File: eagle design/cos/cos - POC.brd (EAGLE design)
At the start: 35 x 63 mm, 103 parts, among them IC1 SQJ952EP-T1_GE3, IC10 PBRC8.00GR50X000, IC11 LM74670QDGKRQ1, IC12 LM74670QDGKRQ1, IC13 SQJ886EP-T1_GE3, IC15 MCP23S08-E/ML, IC16 LDK320M50R, IC17 MCP2515, IC18 LM74670QDGKRQ1, IC19 MCP2561-2, IC2 SQJ952EP-T1_GE3, IC20 AD5160BRJZ5-R2, IC21 MP3221GJ-P, IC3 SQJ952EP-T1_GE3, IC4 TPS630702RNMT, IC5 LM74670QDGKRQ1, IC6 FDMQ8403, IC7 LMP92064SD/NOPB, IC8 ATTINY4313-MMH, IC9 LM74670QDGKRQ1

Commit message: - further layout work
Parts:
- removed TP9: Li-Ion Cell +, testpad:P1-13
- C1, C2: value 10μF -> 3300μF / 35V / ultralow ESR; device rcl:C0805 -> rcl:E1,8-4
- C3: device rcl:C0603 -> rcl:C0805
- C4: value 3300μF / 35V / ultralow ESR -> 10μF; device rcl:E1,8-4 -> rcl:C0805
- C5: value 3300μF / 35V / ultralow ESR -> 10μF; device rcl:E1,8-4 -> rcl:C0603
- IC3: value SQJ952EP-T1_GE3 -> TPS630702RNMT; device SQJ952EP-T1_GE3 - Dual N-Fet:SO-8L -> TPS630701 - Buck Boost 5V regulator:VQFN
- IC4: value TPS630702RNMT -> LM74670QDGKRQ1; device TPS630701 - Buck Boost 5V regulator:VQFN -> LM74670 - Smart Diode Rectifier Controller:VSSOP-8
- IC5: value LM74670QDGKRQ1 -> SQJ952EP-T1_GE3; device LM74670 - Smart Diode Rectifier Controller:VSSOP-8 -> SQJ952EP-T1_GE3 - Dual N-Fet:SO-8L
- R2: value 10k -> 47k
- R4: value 47k -> 100k
- R7: value 100k -> 10k
- moved R4 84.8 mm to (49.5, -20.0), flipped to the top
- moved C3 79.6 mm to (95.2, 33.0), turned to 0 degrees
- moved TP5 78.3 mm to (107.2, 30.8), turned to 270 degrees
- moved C7 77.4 mm to (101.8, 27.2)
- moved L1 77.4 mm to (101.2, 33.0)
- moved R13 77.4 mm to (101.8, 28.5)
- moved TP6 77.0 mm to (107.2, 32.2), turned to 270 degrees
- moved C10 76.6 mm to (104.2, 33.5)
- moved C11 76.6 mm to (106.2, 33.5)
- moved C13 76.6 mm to (108.2, 33.5)
- moved C18 75.7 mm to (107.2, 29.5)
- moved R7 70.3 mm to (96.5, 37.2), flipped to the bottom
- moved IC4 67.2 mm to (105.0, 49.0)
- moved C2 66.1 mm to (103.0, 45.0), turned to 0 degrees
- moved C1 60.9 mm to (107.2, 45.0), turned to 180 degrees
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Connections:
- net 5V0_LDO: now also R3.2; no longer R2.2
- net 5V0_TP-IN: now also IC3.5-FB, IC3.7-VOUT, IC3.8-VOUT, IC3.VOUT; no longer IC4.5-FB, IC4.7-VOUT, IC4.8-VOUT, IC4.VOUT
- net D1_VCAPH: now also IC4.VCAPH; no longer IC5.VCAPH
- net D1_VCAPL: now also IC4.VCAPL; no longer IC5.VCAPL
- net DELON_1: now also IC5.D1_1, IC5.D1_2, IC5.D1_3; no longer IC3.D1_1, IC3.D1_2, IC3.D1_3
- net DYNAMO_2: now also IC5.D2_1, IC5.D2_2, IC5.D2_3; no longer IC3.D2_1, IC3.D2_2, IC3.D2_3
- net DYNAMO_2_C: now also C1.-, IC4.ANODE; no longer C4.-, IC5.ANODE
- net EN: now also IC3.14-EN; no longer IC4.14-EN
- net GATE_D1: now also IC4.GATE_DRIVE, IC4.GATE_PULLD; no longer IC5.GATE_DRIVE, IC5.GATE_PULLD
- net GATE_DELON: now also IC5.G1, IC5.G2, R7.2; no longer IC3.G1, IC3.G2, R3.2
- net GATE_GRAETZ: now also R3.1; no longer R2.1
- net GND: now also C4.2, C5.2, IC3.10-PGND, IC3.15-VSEL, IC3.4-GND, IC3.6-FB2, R7.1; no longer C1.2, C2.2, IC4.10-PGND, IC4.15-VSEL, IC4.4-GND, IC4.6-FB2, R3.1, TP9.TP
- net N$1: now also IC3.11-L1; no longer IC4.11-L1
- net N$14: now also R4.1, R5.2; no longer R5.1, R6.2
- net N$20: now also IC5.S1, IC5.S2; no longer IC3.S1, IC3.S2
- net N$5: now also IC3.9-L2; no longer IC4.9-L2
- net PG: now also IC3.2-PG; no longer IC4.2-PG
- net PS/SYNC: now also IC3.1-PS/S; no longer IC4.1-PS/S
- net TUNING_CAP_DRAIN: now also C2.-; no longer C5.-
- net TUNIN_CAP2_BIAS: now also C1.+, C2.+, R2.1; no longer C4.+, C5.+, R4.1
- net VAUX: now also IC3.3-VAUX; no longer IC4.3-VAUX
- net V_DC_TP-IN: now also IC4.CATHODE, R2.2; no longer IC5.CATHODE, R4.2
- net V_REGULATED_TP-OUT: now also C4.1, C5.1, IC3.12-VIN, IC3.13-VIN, IC3.VIN; no longer C1.1, C2.1, IC4.12-VIN, IC4.13-VIN, IC4.VIN
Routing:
- net DYNAMO_2: track 19.0 -> 42.5 mm, vias 9 -> 10
- net V_REGULATED_TP-IN: track 15.3 -> 38.7 mm, vias 7 -> 6
- net DYNAMO_2_C: track 40.9 -> 63.3 mm
- net V_DC_TP-OUT: track 9.54 -> 20.7 mm, vias 0 -> 2
- net GATE_TUNING-CAP: track 4.27 -> 12.3 mm
- net GATE_GRAETZ: track 4.27 -> 11.7 mm
- net V_LI-ION_BATTERY: track 7.71 -> 15.1 mm
- net GATE_DELON: track 4.27 -> 11.4 mm
- net V_REGULATED_TP-OUT: track 5.35 -> 11.6 mm
- net TUNING_CAP_DRAIN: track 8.30 -> 12.8 mm
- net DELON_1: track 9.80 -> 14.0 mm
- net V_DC_TP-IN: track 31.1 -> 34.4 mm
- net 5V0_TP-IN: track 14.5 -> 17.8 mm, vias 3 -> 4
- net DYNAMO_1: track 23.4 -> 26.4 mm
- net IDEAL_DIODE_GATE: track 6.52 -> 9.50 mm
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
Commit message: - further work on schematic
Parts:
- removed C22: 0.1μF, rcl:C0402
- removed IC11: LM74670QDGKRQ1, LM74670 - Smart Diode Rectifier Controller:VSSOP-8
- removed IC13: SQJ886EP-T1_GE3, SQJ886EP - N-FET:SO-8L
- added C36, C37: 0.1μF, rcl:C0402
- added IC22: SQJ952EP-T1_GE3, SQJ952EP-T1_GE3 - Dual N-Fet:SO-8L
- added IC23, IC24: LM74670QDGKRQ1, LM74670 - Smart Diode Rectifier Controller:VSSOP-8
- IC14: value (none) -> MCP73871-2CCI/ML
- moved TP11 16.0 mm to (86.2, 45.2)
- moved TP12 16.0 mm to (86.2, 43.8)
- moved D5 0.75 mm to (111.2, 31.5)
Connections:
- removed net D5_VCAPH: C22.2, IC11.VCAPH
- removed net D5_VCAPL: C22.1, IC11.VCAPL
- removed net DYNAMO_2: D3.A, IC1.D2_1, IC1.D2_2, IC1.D2_3, IC2.D1_1, IC2.D1_2, IC2.D1_3, IC5.D2_1, IC5.D2_2, IC5.D2_3
- removed net DYNAMO_2_C: C1.-, D1.A, IC2.D2_1, IC2.D2_2, IC2.D2_3, IC4.ANODE, IC6.3_S1/D2, IC6.S1/D2, IC9.CATHODE, TP1.TP
- removed net IDEAL_DIODE_GATE: IC11.GATE_DRIVE, IC11.GATE_PULLD, IC13.G
- removed net TUNING_CAP_DRAIN: C2.-, IC1.D1_1, IC1.D1_2, IC1.D1_3
- new net AFTER_SW_BEFORE_TUNING_CAP: C1.-, IC1.D2_1, IC1.D2_2, IC1.D2_3
- new net DYNAMO_2_AFTER_SW: C2.-, D3.A, IC2.D1_1, IC2.D1_2, IC2.D1_3, IC5.D2_1, IC5.D2_2, IC5.D2_3
- new net DYNAMO_2_BEFORE_SW: D1.A, IC1.D1_1, IC1.D1_2, IC1.D1_3, IC2.D2_1, IC2.D2_2, IC2.D2_3, IC4.ANODE, IC6.3_S1/D2, IC6.S1/D2, IC9.CATHODE, TP1.TP
- new net D_SMOOTH_VCAP: C36.1, IC23.VCAPL
- new net D_SMOOTH_VCAPH: C36.2, IC23.VCAPH
- new net D_VLIION_VCAPH: C37.2, IC24.VCAPH
- new net D_VLIION_VCAPL: C37.1, IC24.VCAPL
- new net GATE_DIODE_SMOOTH: IC22.G1, IC23.GATE_DRIVE, IC23.GATE_PULLD
- new net GATE_DIODE_V_LIION: IC22.G2, IC24.GATE_DRIVE, IC24.GATE_PULLD
- net V_DC_TP-OUT: now also IC22.S1, IC23.ANODE; no longer IC11.ANODE, IC13.S1, IC13.S2, IC13.S3
- net V_LI-ION_BATTERY: now also IC22.S2, IC24.ANODE
- net V_REGULATED_TP-IN: now also IC23.CATHODE; no longer IC11.CATHODE, IC13.D1, IC13.D2
- net V_REGULATED_TP-OUT: now also IC22.D1_1, IC22.D1_2, IC22.D1_3, IC22.D2_1, IC22.D2_2, IC22.D2_3, IC24.CATHODE
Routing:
- net DYNAMO_2_C: track 63.3 -> 0.00 mm, vias 8 -> 0
- net DYNAMO_2_BEFORE_SW: track 0.00 -> 50.9 mm, vias 0 -> 5
- net DYNAMO_2: track 42.5 -> 0.00 mm, vias 10 -> 0
- net DYNAMO_2_AFTER_SW: track 0.00 -> 39.2 mm, vias 0 -> 10
- net V_REGULATED_TP-IN: track 38.7 -> 0.11 mm, vias 6 -> 0
- net V_DC_TP-OUT: track 20.7 -> 0.00 mm, vias 2 -> 0
- net V_REGULATED_TP-OUT: track 11.6 -> 26.5 mm
- net TUNING_CAP_DRAIN: track 12.8 -> 0.00 mm, vias 3 -> 0
- net IDEAL_DIODE_GATE: track 9.50 -> 0.00 mm, vias 2 -> 0
- net GATE_DIODE_SMOOTH: track 0.00 -> 7.38 mm
- net GATE_DIODE_V_LIION: track 0.00 -> 7.03 mm
- net V_LI-ION_BATTERY: track 15.1 -> 17.5 mm
- net D5_VCAPL: track 2.27 -> 0.00 mm, vias 1 -> 0
- net D5_VCAPH: track 1.65 -> 0.00 mm, vias 1 -> 0
- net COMP_IN: track 3.24 -> 2.49 mm

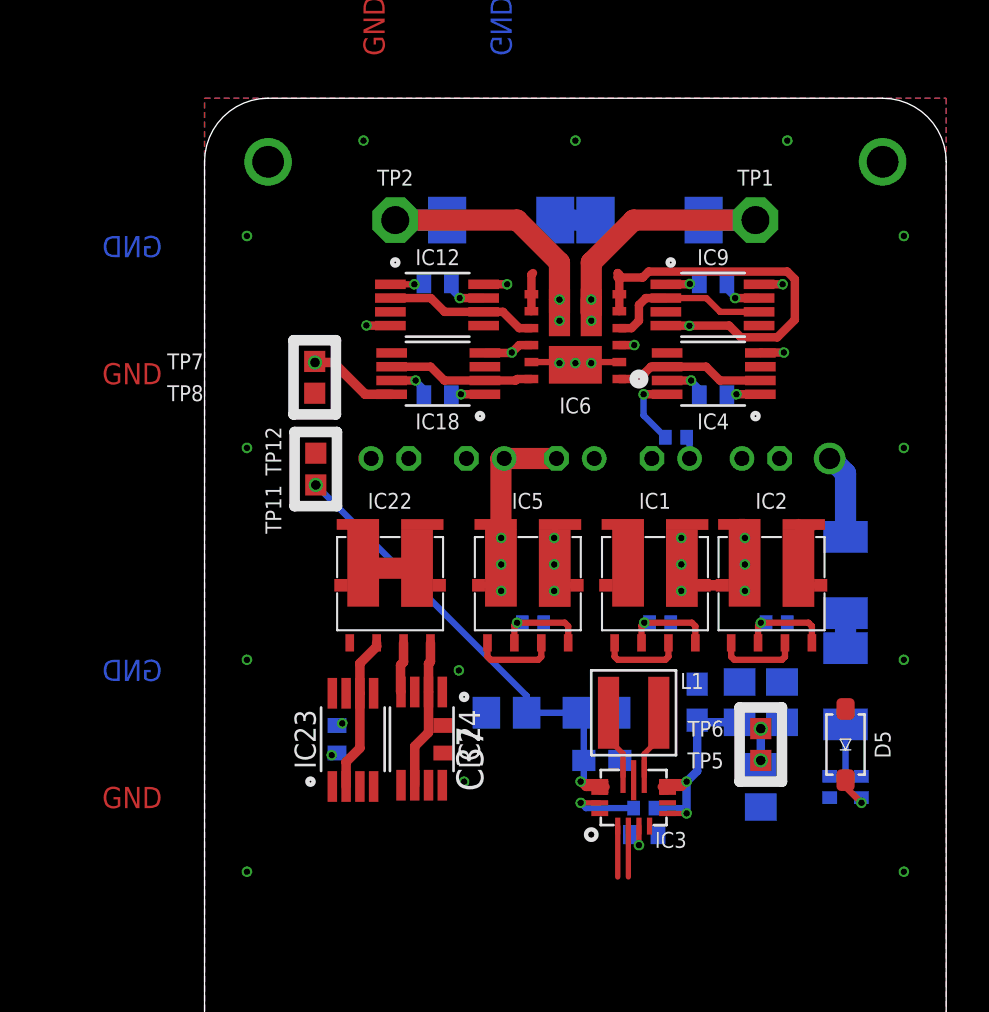
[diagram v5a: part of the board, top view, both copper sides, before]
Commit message: - further work on schematic:routed bridge rectifier segment - added TPS630701 - Buck-Boost Converter 5V out fixed datasheet
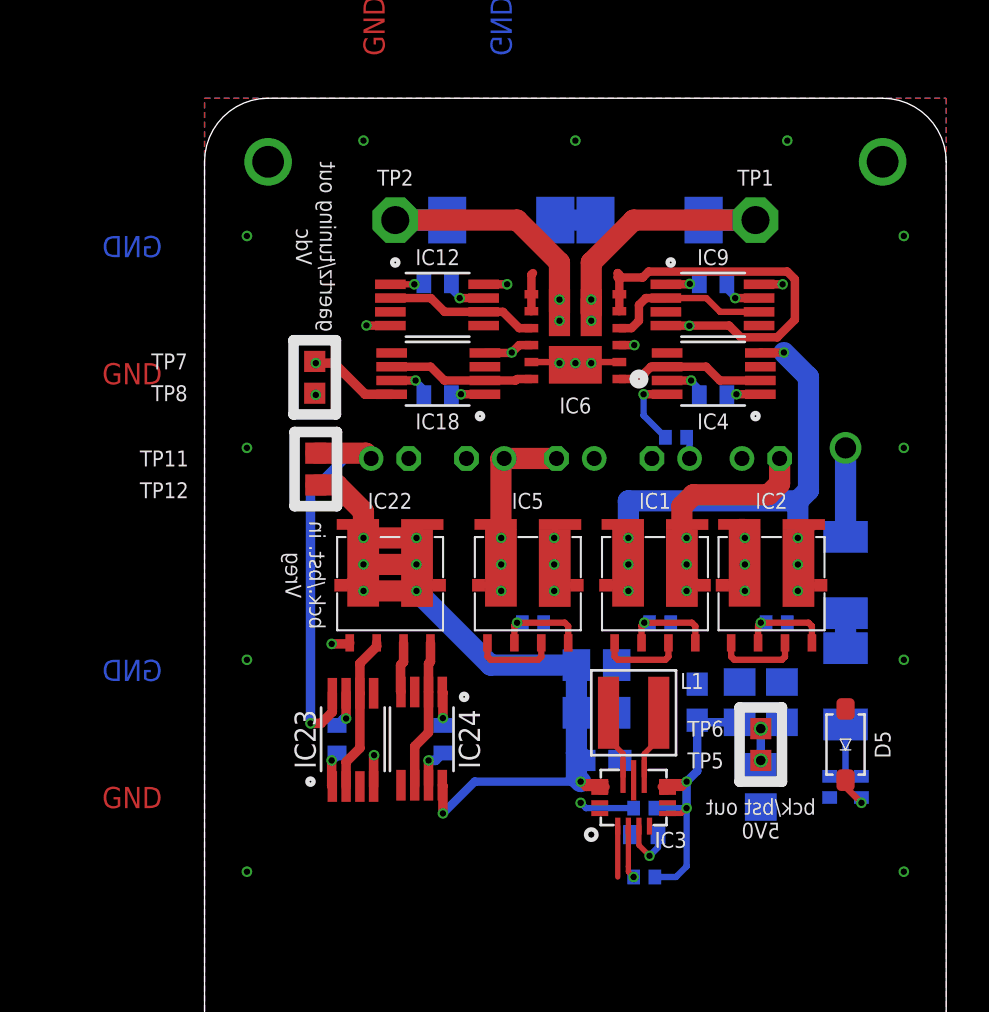
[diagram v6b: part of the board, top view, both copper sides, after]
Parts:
- added R27: 100k, rcl:R0402
- moved C3 4.81 mm to (99.5, 35.2), turned to 180 degrees
- flipped C37 to the bottom
- turned C7 to 0 degrees
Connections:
- new net EN2: IC21.4_EN, R23.1
- net 5V0_TP-IN: now also R27.2
- net EN: no longer IC21.4_EN, IC3.14-EN, R23.1
- net PG: now also R27.1
- net V_REGULATED_TP-OUT: now also IC3.14-EN
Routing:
- net V_REGULATED_TP-OUT: track 26.5 -> 52.4 mm, vias 2 -> 8
- net V_DC_TP-OUT: track 0.00 -> 20.5 mm, vias 0 -> 3
- net V_REGULATED_TP-IN: track 0.11 -> 19.3 mm, vias 0 -> 1
- net AFTER_SW_BEFORE_TUNING_CAP: track 0.00 -> 15.5 mm, vias 0 -> 3
- net DYNAMO_2_BEFORE_SW: track 50.9 -> 59.8 mm, vias 5 -> 11
- net 5V0_TP-IN: track 18.0 -> 22.2 mm
- net D_VLIION_VCAPH: track 0.00 -> 1.99 mm, vias 0 -> 1
- net EN: track 4.47 -> 2.60 mm, vias 2 -> 1
- net D_SMOOTH_VCAPH: track 0.00 -> 1.76 mm, vias 0 -> 1
- net D_SMOOTH_VCAP: track 0.00 -> 1.70 mm, vias 0 -> 1
- net D_VLIION_VCAPL: track 0.00 -> 1.59 mm, vias 0 -> 1
- net VAUX: track 1.57 -> 2.77 mm
- net EN2: track 0.00 -> 0.97 mm, vias 0 -> 1
- net DYNAMO_2_AFTER_SW: track 39.2 -> 39.8 mm, vias 10 -> 7
- net V_DC_TP-IN: track 34.4 -> 34.9 mm
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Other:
- board text added: "bck./bst. in Vreg"
- board text added: "bck/bst out 5V0"
- board text added: "gaertz/tuning out Vdc"

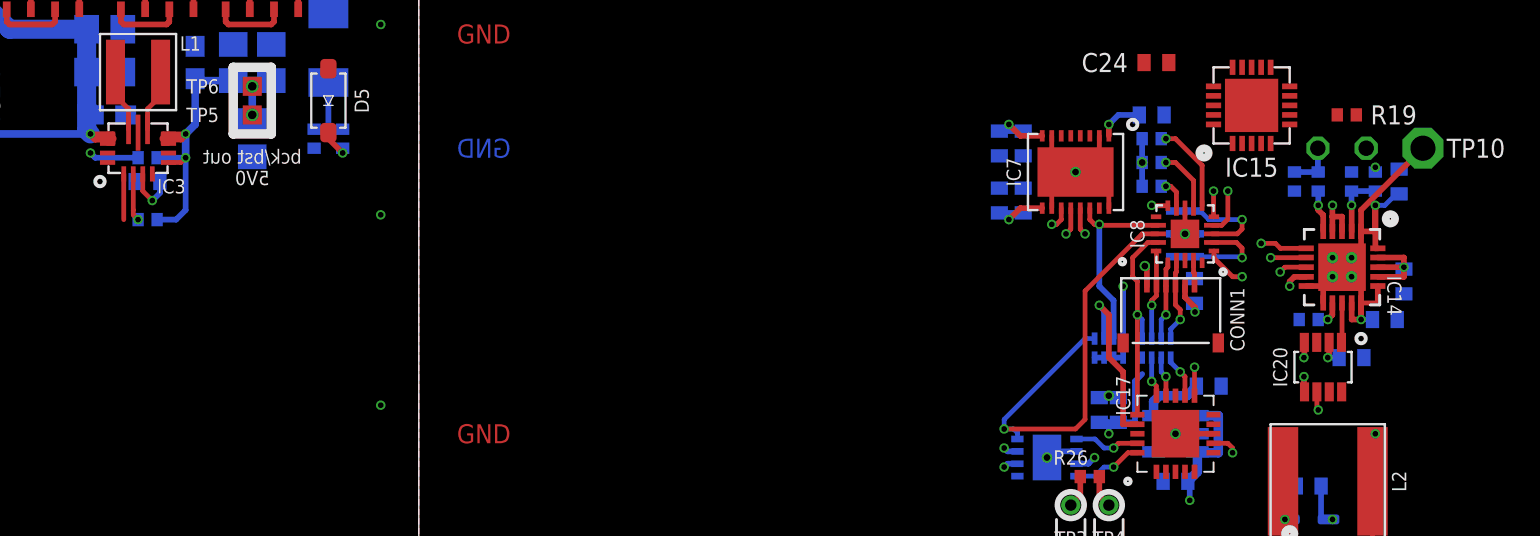
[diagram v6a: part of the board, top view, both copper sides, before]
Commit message: - further work on schematic: reassigned ps/sync to a 16bit timer capable GPIO
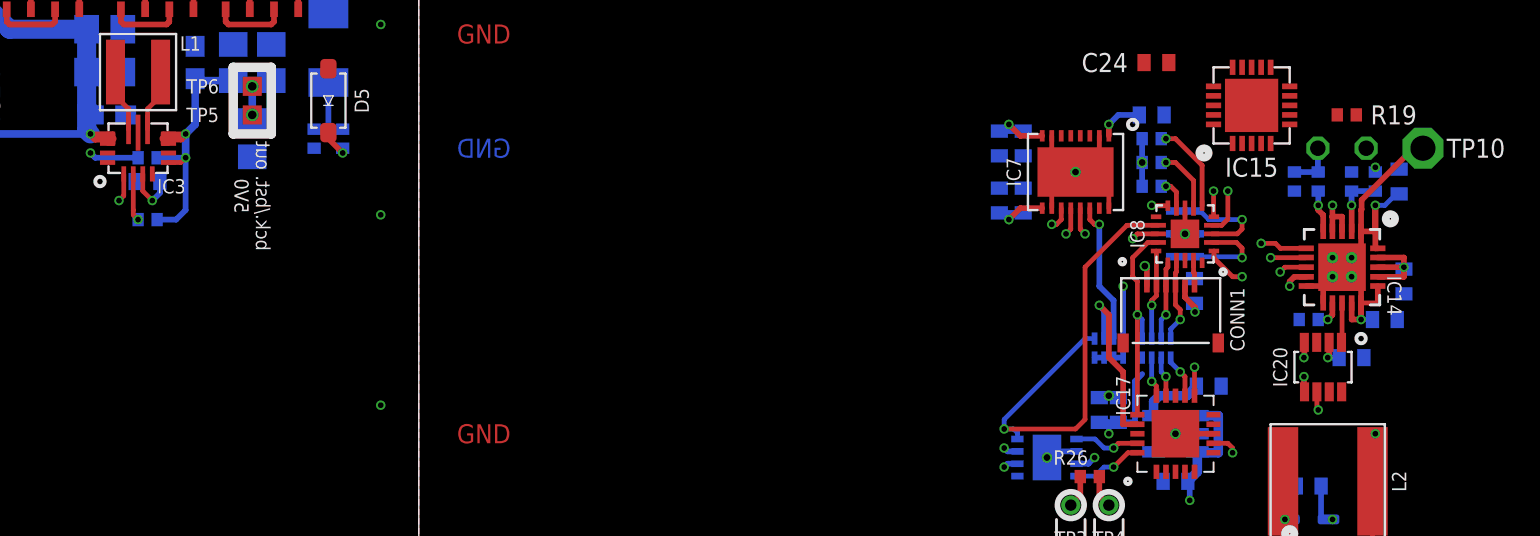
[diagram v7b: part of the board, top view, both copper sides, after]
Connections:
- removed net MCP23S08_GP7: IC15.16_GP7
- net LMP92064SD_CS: now also IC15.16_GP7; no longer IC8.12
- net PS/SYNC: now also IC8.13
- net STBY: now also IC8.12; no longer IC8.13
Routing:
- net PS/SYNC: track 2.40 -> 12.9 mm, vias 0 -> 2
- net LMP92064SD_CS: track 10.6 -> 7.58 mm
- net STBY: track 24.4 -> 25.3 mm
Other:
- board text added: "bck./bst. out 5V0"
- board text removed: "bck/bst out 5V0"
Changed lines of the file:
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@@
 <text x="102" y="-3" size="1" layer="16" font="vector" rot="MR90" align="center-right">GND</text>
 <text x="106" y="-3" size="1" layer="2" font="vector" rot="R90" align="center-right">GND</text>
-<text x="107.25" y="28" size="0.75" layer="21" rot="MR0" align="center">bck/bst out
+<text x="107.25" y="26.5" size="0.75" layer="21" rot="MR270" align="center">bck./bst. out
 5V0</text>
 <text x="85.75" y="39.5" size="0.75" layer="21" rot="MR270" align="center">bck./bst. in
@@
 <wire x1="151" y1="19" x2="146.75" y2="14.75" width="0.25" layer="16"/>
 <wire x1="146.75" y1="14.75" x2="146.75" y2="14.25" width="0.25" layer="16"/>
-<contactref element="IC8" pad="13"/>
-<wire x1="154.85" y1="24.5" x2="154" y2="24.5" width="0.25" layer="1"/>
-<wire x1="151" y1="21.5" x2="154" y2="24.5" width="0.25" layer="1"/>
 <wire x1="146.75" y1="14.25" x2="150.5" y2="14.25" width="0.25" layer="1"/>
 <wire x1="150.5" y1="14.25" x2="151" y2="14.75" width="0.25" layer="1"/>
-<wire x1="151" y1="14.75" x2="151" y2="21.5" width="0.25" layer="1"/>
+<wire x1="151" y1="22.75" x2="151" y2="14.75" width="0.25" layer="1"/>
+<contactref element="IC8" pad="12"/>
+<wire x1="154.85" y1="24.95" x2="153.2" y2="24.95" width="0.25" layer="1"/>
+<wire x1="153.2" y1="24.95" x2="151" y2="22.75" width="0.25" layer="1"/>
 </signal>
 <signal name="5V0_TP-OUT" class="2">
@@
 <wire x1="166.1" y1="20" x2="165.5" y2="20" width="0.254" layer="16"/>
 <contactref element="TP10" pad="TP"/>
-<wire x1="168.75" y1="29" x2="165.5" y2="25.75" width="0.3" layer="1"/>
-<wire x1="165.5" y1="20" x2="165.5" y2="25.75" width="0.3" layer="1"/>
+<wire x1="168.25" y1="29" x2="168.75" y2="29" width="0.3" layer="1"/>
 <contactref element="IC22" pad="S2"/>
 <contactref element="IC24" pad="ANODE"/>
@@
 <wire x1="90.25" y1="35.25" x2="90.25" y2="34" width="0.45" layer="1"/>
 <wire x1="90.25" y1="34" x2="90.27" y2="33.98" width="0.45" layer="1"/>
+<wire x1="165.5" y1="25.75244375" x2="165.5286" y2="25.78104375" width="0.3" layer="1"/>
+<wire x1="165.5" y1="20" x2="165.5" y2="25.75244375" width="0.3" layer="1"/>
+<wire x1="165.5286" y1="26.2786" x2="168.25" y2="29" width="0.3" layer="1"/>
+<wire x1="165.5286" y1="25.78104375" x2="165.5286" y2="26.2786" width="0.3" layer="1"/>
 <wire x1="165.4906" y1="20" x2="165.5" y2="20" width="0" layer="19" extent="1-16"/>
-<wire x1="90.27" y1="33.98" x2="165.5" y2="25.75" width="0" layer="19" extent="1-1"/>
+<wire x1="90.25" y1="34" x2="165.5286" y2="26.2786" width="0" layer="19" extent="1-1"/>
 </signal>
 <signal name="V_LI-ION_OUT">
@@
 <signal name="LMP92064SD_CS">
 <contactref element="IC7" pad="14_CSB"/>
-<contactref element="IC8" pad="12"/>
-<wire x1="151.8" y1="24.95" x2="154.85" y2="24.95" width="0.254" layer="1"/>
 <via x="151.75" y="25" extent="1-16" drill="0.3"/>
 <wire x1="151.75" y1="25" x2="151.5" y2="25" width="0.254" layer="1"/>
@@
 <contactref element="R18" pad="6"/>
 <wire x1="152.5" y1="19" x2="152.5" y2="21" width="0.3" layer="16"/>
+<contactref element="IC15" pad="16_GP7"/>
+<wire x1="151.25" y1="25.85" x2="157.75" y2="32.25" width="0" layer="19" extent="1-1"/>
 </signal>
 <signal name="N$10">
@@
 <signal name="PS/SYNC" class="3">
 <contactref element="IC3" pad="1-PS/S"/>
-<wire x1="100.5" y1="27.65" x2="100.5" y2="25.25" width="0.254" layer="1"/>
+<contactref element="IC8" pad="13"/>
+<via x="153.5" y="24.25" extent="1-16" drill="0.3"/>
+<wire x1="153.5" y1="24.25" x2="153.75" y2="24.5" width="0.25" layer="1"/>
+<wire x1="153.75" y1="24.5" x2="154.85" y2="24.5" width="0.25" layer="1"/>
+<wire x1="153.5" y1="24.25" x2="153" y2="24.75" width="0.4" layer="2"/>
+<wire x1="153" y1="24.75" x2="153" y2="31.75" width="0.4" layer="2"/>
+<via x="100.25" y="26.25" extent="1-16" drill="0.3"/>
+<wire x1="100.5" y1="27.65" x2="100.5" y2="26.5" width="0.25" layer="1"/>
+<wire x1="100.5" y1="26.5" x2="100.25" y2="26.25" width="0.25" layer="1"/>
+<wire x1="100.25" y1="26.25" x2="100.25" y2="24" width="0.4" layer="2"/>
+<wire x1="100.5" y1="26.5" x2="153" y2="24.75" width="0" layer="19" extent="1-2"/>
 </signal>
 <signal name="PG" class="3">
@@
 <contactref element="IC15" pad="15_GP6"/>
 </signal>
-<signal name="MCP23S08_GP7">
-<contactref element="IC15" pad="16_GP7"/>
-</signal>
 <signal name="5V9_LDO">
